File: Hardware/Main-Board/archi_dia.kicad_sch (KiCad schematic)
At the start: 0 parts

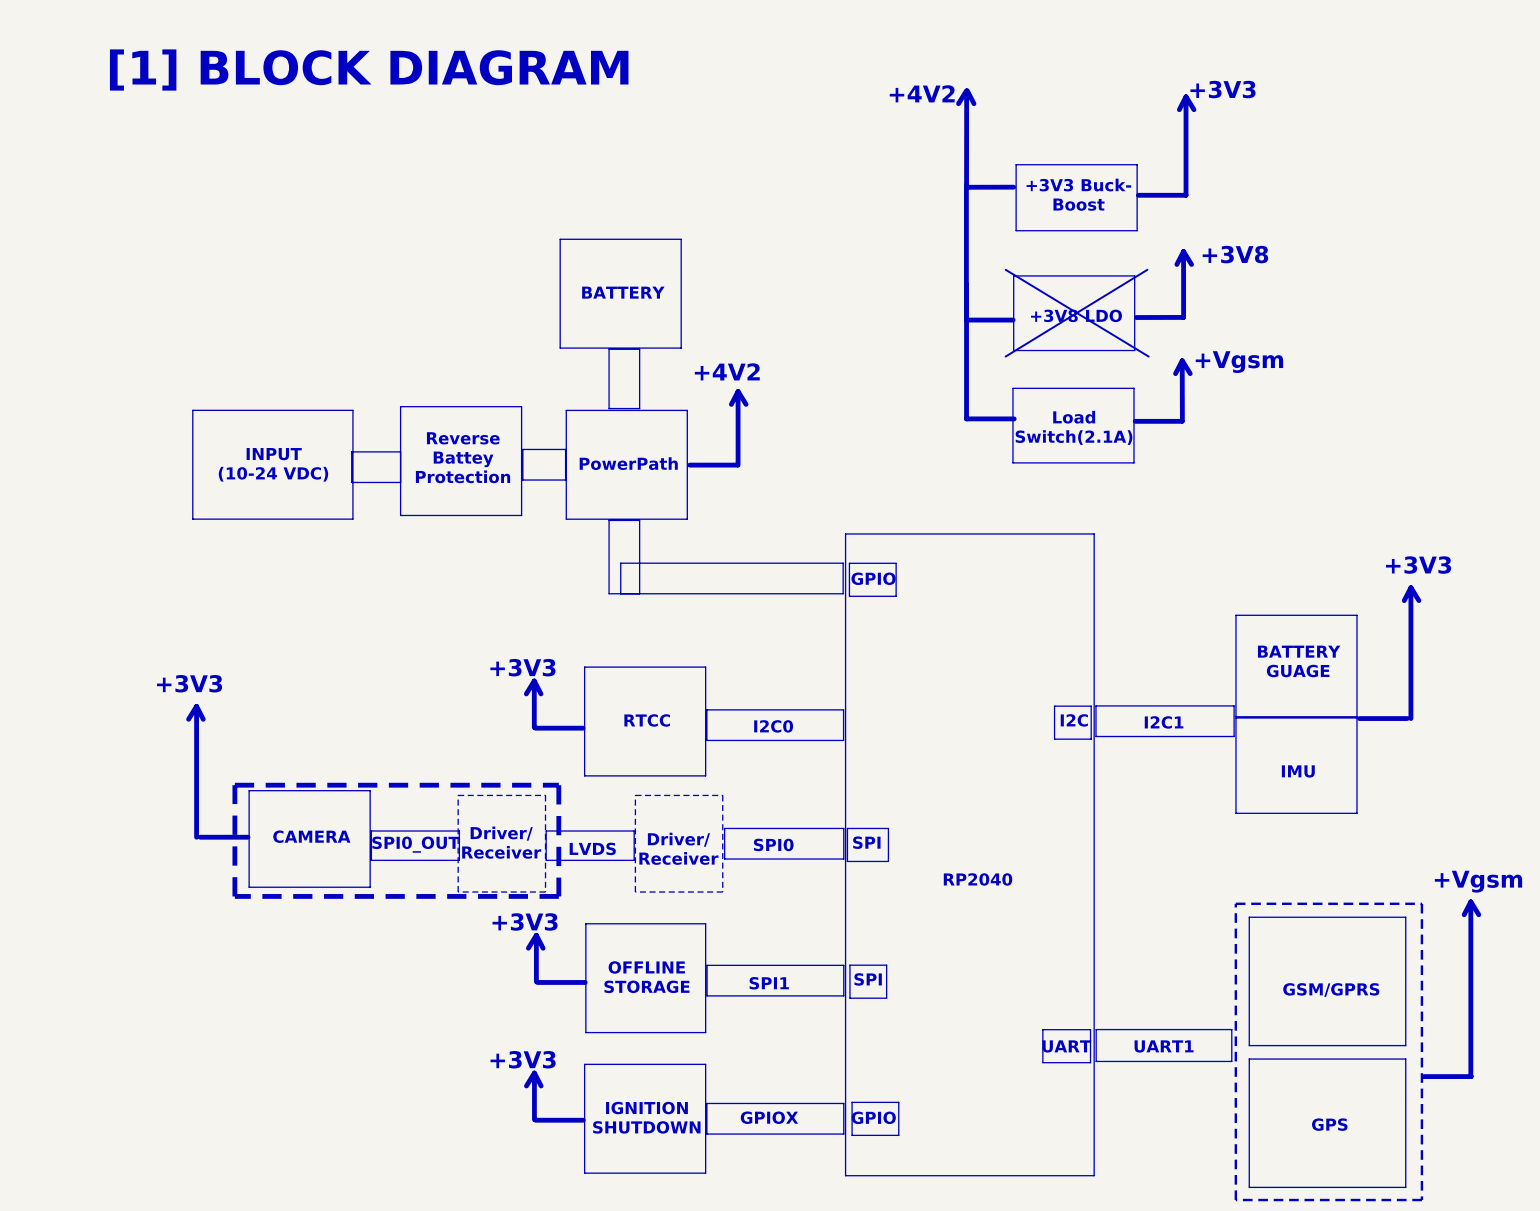
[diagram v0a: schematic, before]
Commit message: Done with main board design, and camera interconnect in progress
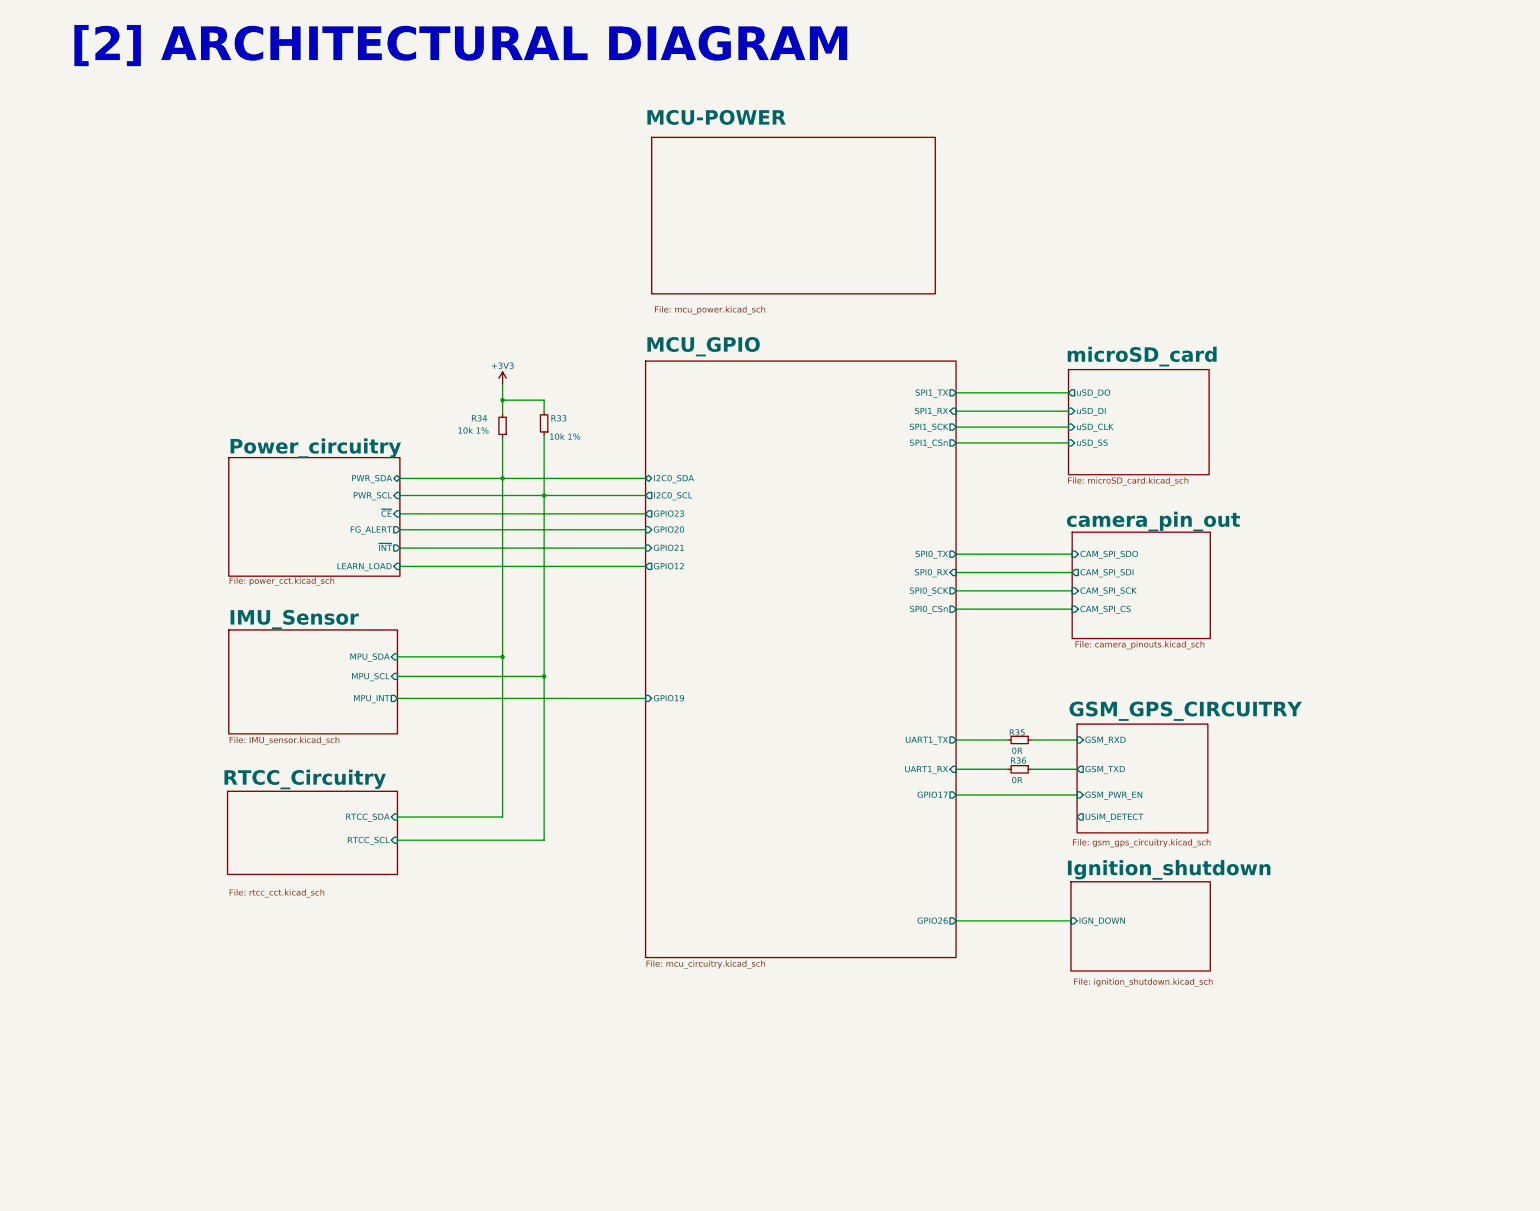
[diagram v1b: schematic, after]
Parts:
- added R33, R34: 10k 1%, Resistor_SMD:R_0402_1005Metric, symbol Device:R_Small
- added R35, R36: 0R, Resistor_SMD:R_0402_1005Metric, symbol Device:R_Small
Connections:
- new net +3V3: R33.2, R34.2
- new net GSM_GPS_CIRCUITRY/GSM_RXD: R35.1
- new net GSM_GPS_CIRCUITRY/GSM_TXD: R36.1
- new net IMU_Sensor/MPU_SCL: R33.1
- new net IMU_Sensor/MPU_SDA: R34.1
- new net MCU_GPIO/UART1_RX: R36.2
- new net MCU_GPIO/UART1_TX: R35.2
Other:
- added sheet GSM_GPS_CIRCUITRY (gsm_gps_circuitry.kicad_sch)
- added sheet IMU_Sensor (IMU_sensor.kicad_sch)
- added sheet Ignition_shutdown (ignition_shutdown.kicad_sch)
- added sheet MCU-POWER (mcu_power.kicad_sch)
- added sheet MCU_GPIO (mcu_circuitry.kicad_sch)
- added sheet Power_circuitry (power_cct.kicad_sch)
- added sheet RTCC_Circuitry (rtcc_cct.kicad_sch)
- added sheet camera_pin_out (camera_pinouts.kicad_sch)
- added sheet microSD_card (microSD_card.kicad_sch)
- note added: "[2] ARCHITECTURAL DIAGRAM"
- note removed: "+3V3"
- note removed: "+3V3 Buck- Boost"
- note removed: "+3V8"
- note removed: "+3V8 LDO"
- note removed: "+4V2"
- note removed: "+Vgsm"
- note removed: "BATTERY"
- note removed: "BATTERY GUAGE"
- note removed: "CAMERA"
- note removed: "Driver/ Receiver"
- note removed: "GPIO"
- note removed: "GPIOX"
- note removed: "GPS"
- note removed: "GSM/GPRS"
- note removed: "I2C"
- note removed: "I2C0"
- note removed: "I2C1"
- note removed: "IGNITION SHUTDOWN"
- note removed: "IMU"
- note removed: "INPUT (10-24 VDC)"
- note removed: "LVDS"
- note removed: "Load Switch(2.1A)"
- note removed: "OFFLINE STORAGE"
- note removed: "PowerPath"
- note removed: "RP2040"
- note removed: "RTCC"
- note removed: "Reverse Battey Protection"
- note removed: "SPI"
- note removed: "SPI0"
- note removed: "SPI0_OUT"
- note removed: "SPI1"
- note removed: "UART"
- note removed: "UART1"
- note removed: "[1] BLOCK DIAGRAM"
